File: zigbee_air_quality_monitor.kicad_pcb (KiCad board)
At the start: 2 copper layers, 21 parts, among them J1 USB_C_Receptacle_USB2.0, J2 Conn_02x02_Odd_Even, SW1 PWR_BTN, U1 BT840, U2 PRTR5V0U2F, U3 XC6206P332MR, U4 SCD41-D-R2

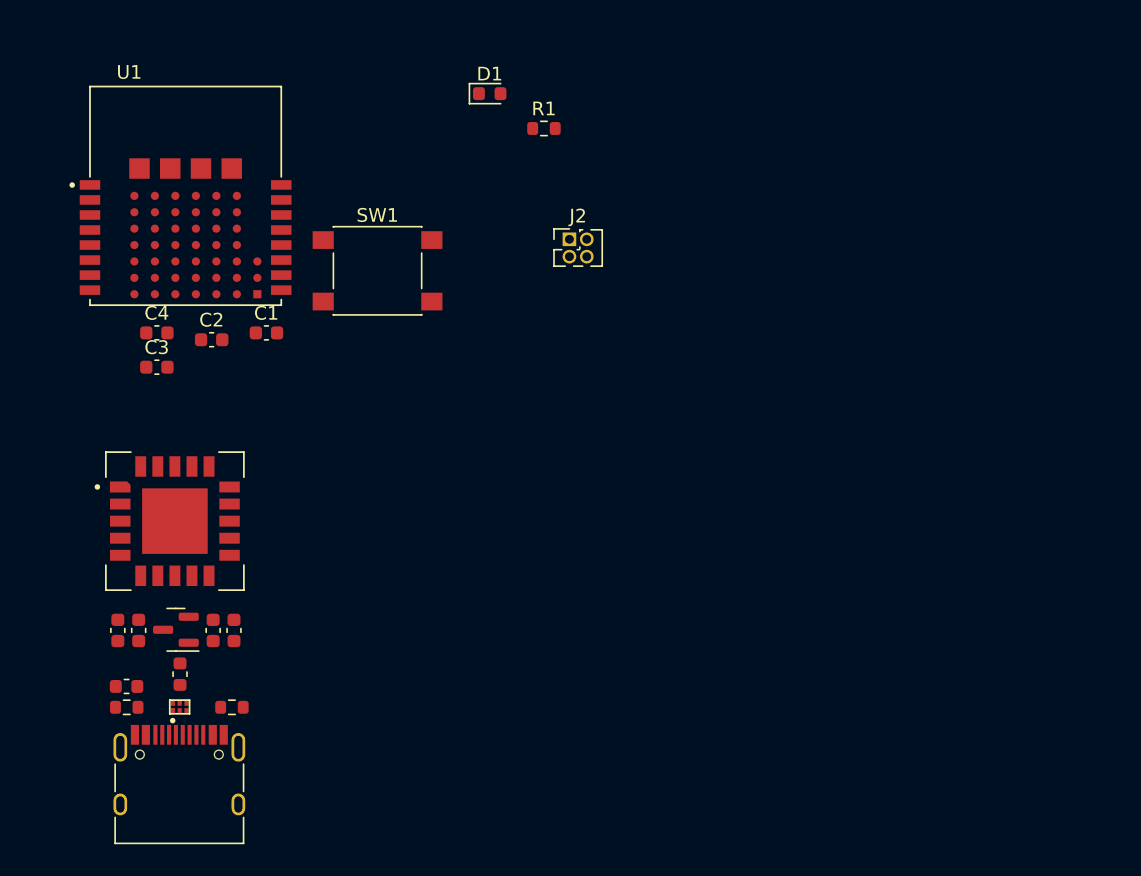
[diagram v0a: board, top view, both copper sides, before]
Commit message: Finished schematics, added 3D models
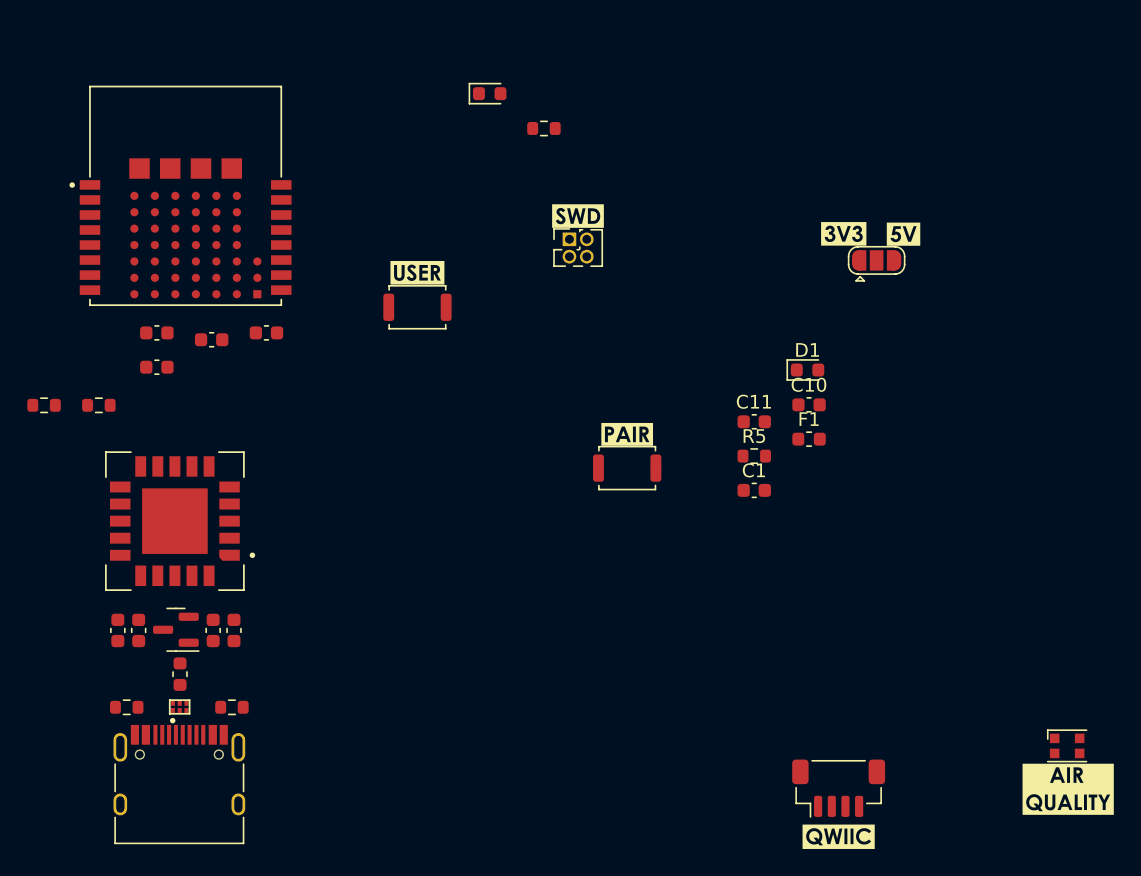
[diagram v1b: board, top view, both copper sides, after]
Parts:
- added C1: 100nF, Capacitor_SMD:C_0603_1608Metric, F.Cu at (174.0, 115.2)
- added C10: 100nF, Capacitor_SMD:C_0603_1608Metric, F.Cu at (178.0, 109.0)
- added C11: 4.7uF, Capacitor_SMD:C_0603_1608Metric, F.Cu at (174.0, 110.2)
- added D1: STATUS_LED, LED_SMD:LED_0603_1608Metric, F.Cu at (177.9, 106.4)
- added D3: WS2812B, LED_SMD:LED_WS2812B-2020_PLCC4_2.0x2.0mm, F.Cu at (196.9, 133.9)
- added J3: QWIIC, Connector_JST:JST_SH_BM04B-SRSS-TB_1x04-1MP_P1.00mm_Vertical, F.Cu at (180.2, 137.0)
- added JP1: SolderJumper_3_Bridged12, Jumper:SolderJumper-3_P1.3mm_Open_RoundedPad1.0x1.5mm, F.Cu at (183.0, 98.4)
- added R3: 5k1, Resistor_SMD:R_0603_1608Metric, F.Cu at (122.0, 109.0)
- added R4: 5k1, Resistor_SMD:R_0603_1608Metric, F.Cu at (126.1, 109.0)
- added R5: 1k, Resistor_SMD:R_0603_1608Metric, F.Cu at (174.0, 112.7)
- added SW2: USER_BTN, Button_Switch_SMD:SW_Push_SPST_NO_Alps_SKRK, F.Cu at (149.4, 101.8)
- added kibuzzard-63D64107: G***, kibuzzard-63D64107, F.Cu at (161.1, 95.2)
- added kibuzzard-63D6450F: G***, kibuzzard-63D6450F, F.Cu at (180.2, 140.6)
- added kibuzzard-63D64589: G***, kibuzzard-63D64589, F.Cu at (197.0, 137.1)
- added kibuzzard-63D645FF: G***, kibuzzard-63D645FF, F.Cu at (180.6, 96.5)
- added kibuzzard-63D6461A: G***, kibuzzard-63D6461A, F.Cu at (184.9, 96.5)
- added kibuzzard-63D64B66: G***, kibuzzard-63D64B66, F.Cu at (149.4, 99.3)
- added kibuzzard-63D64B8B: G***, kibuzzard-63D64B8B, F.Cu at (164.7, 111.1)
- D2: renamed from D1; value STATUS_LED -> PAIRING_LED
- SW1: value PWR_BTN -> PAIR_BTN; footprint Button_Switch_SMD:SW_Push_1P1T_NO_6x6mm_H9.5mm -> Button_Switch_SMD:SW_Push_SPST_NO_Alps_SKRK
- moved F1 53.1 mm to (178.0, 111.5)
- moved SW1 23.3 mm to (164.7, 113.6)
- turned U4 to 180 degrees
- renumbered C1 to C2, C2 to C3, C3 to C4, C4 to C6, C6 to C7, C7 to C8, C8 to C9, R2 to R1, R3 to R2, R1 to R6, U2 to U1, U1 to U2
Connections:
- net Net-(R1-Pad1) renamed /PAIRING_LED
- C2 pad 1: Net-(C1-Pad1) -> Net-(C2-Pad1)
- C5 pad 1: Net-(C5-Pad1) -> VCC
- C7 pad 1: Net-(C5-Pad1) -> VCC
- FB1 pad 2: Net-(C5-Pad1) -> VCC
- SW1 pad 1: Net-(C1-Pad1) -> Net-(U2-Pad5)
- U2 pad 1: unconnected-(U1-Pad1) -> /I2C_SDA
- U2 pad 14: /RESET -> unconnected-(U2-Pad14)
- U2 pad 2: unconnected-(U1-Pad2) -> /I2C_SCL
- U2 pad 4: unconnected-(U1-Pad4) -> /AIR_QUALITY_LED
- U2 pad 5: unconnected-(U1-Pad5) -> Net-(U2-Pad5)
- U2 pad 6: Net-(C1-Pad1) -> Net-(C2-Pad1)
- U2 pad 7: unconnected-(U1-Pad7) -> /STATUS_LED
- U3 pad 3: Net-(C5-Pad1) -> VCC
- U4 pad 10: unconnected-(U4-Pad10) -> /I2C_SDA
- U4 pad 19: unconnected-(U4-Pad19) -> VCC
- U4 pad 20: Net-(U4-Pad20) -> GND
- U4 pad 21: Net-(U4-Pad20) -> GND
- U4 pad 6: Net-(U4-Pad20) -> GND
- U4 pad 7: unconnected-(U4-Pad7) -> VCC
- U4 pad 9: unconnected-(U4-Pad9) -> /I2C_SCL

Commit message: Rough part placement
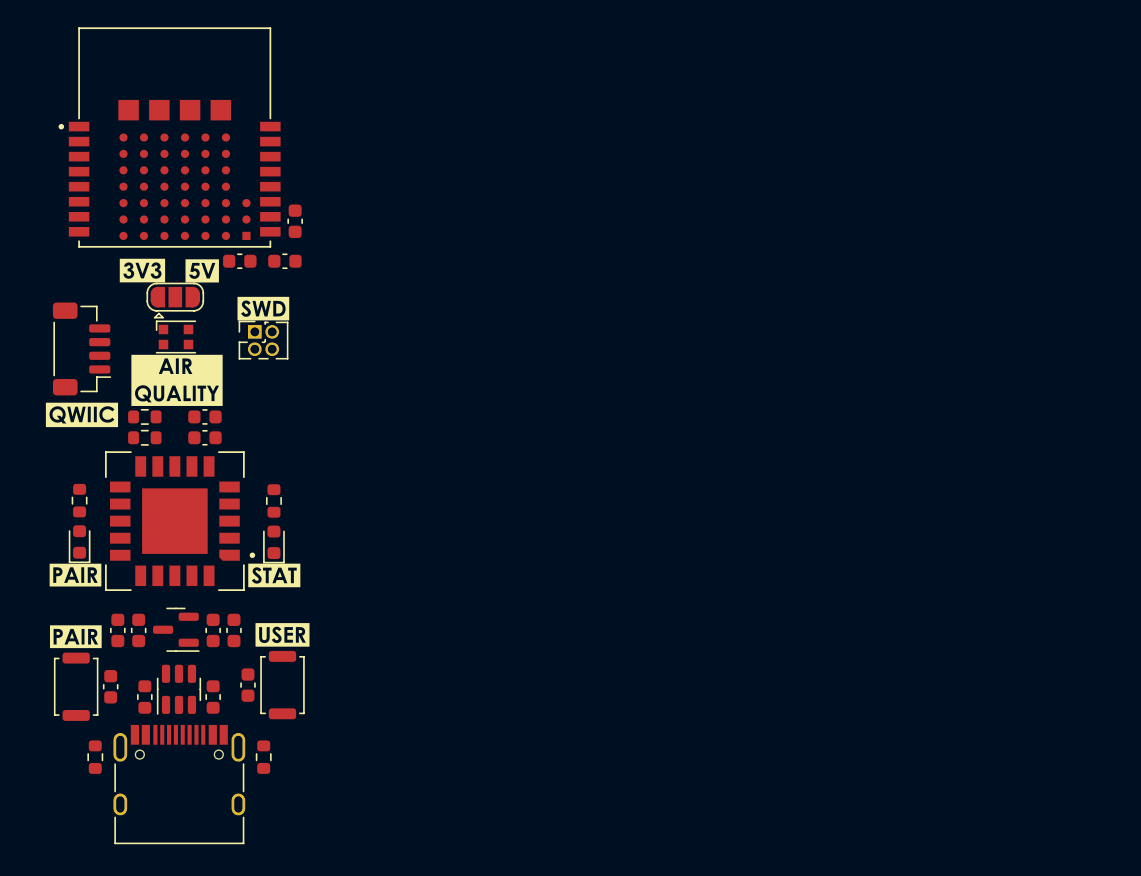
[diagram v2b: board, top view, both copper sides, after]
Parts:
- added kibuzzard-63D64B8B: G***, kibuzzard-63D64B8B, F.Cu at (124.3, 121.4)
- added kibuzzard-63D9ACF8: G***, kibuzzard-63D9ACF8, F.Cu at (138.9, 121.5)
- U1: value PRTR5V0U2F -> USBLC6-2SC6; footprint zigbee_air_quality_monitor:PSON50P145X100X90-6N -> Package_TO_SOT_SMD:SOT-23-6
- moved D3 71.8 mm to (131.7, 104.0)
- moved kibuzzard-63D64589 71.8 mm to (131.8, 107.2)
- moved J2 64.1 mm to (124.8, 104.9), turned to 90 degrees
- moved kibuzzard-63D6450F 63.4 mm to (124.8, 109.7)
- moved F1 52.1 mm to (129.4, 130.3), turned to 90 degrees
- moved JP1 51.4 mm to (131.7, 101.1)
- moved kibuzzard-63D645FF 51.4 mm to (129.2, 99.1)
- moved kibuzzard-63D6461A 51.4 mm to (133.6, 99.2)
- moved C1 49.2 mm to (126.9, 129.6), turned to -90 degrees
- moved D2 44.5 mm to (124.7, 119.0), turned to 90 degrees
- moved C10 44.3 mm to (133.8, 111.4)
- moved R6 43.6 mm to (124.7, 116.0), turned to 90 degrees
- moved SW1 43.4 mm to (124.4, 129.6), turned to -90 degrees
- moved kibuzzard-63D64B8B 43.0 mm to (124.4, 125.9)
- moved D1 41.0 mm to (138.9, 119.0), turned to 90 degrees
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- renumbered J3 to J2, J2 to J3
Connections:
- C3 pad 1: VBUS -> VCC
- U2 pad F6: VBUS -> VCC
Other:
- copper layers 2 -> 4

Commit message: Routing WIP
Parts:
- removed JP1: SolderJumper_3_Bridged12, Jumper:SolderJumper-3_P1.3mm_Open_RoundedPad1.0x1.5mm
- removed kibuzzard-63D645FF: G***, kibuzzard-63D645FF
- removed kibuzzard-63D6461A: G***, kibuzzard-63D6461A
- moved C3 2.80 mm to (136.4, 101.3)
- moved C4 2.80 mm to (140.4, 98.3)
- moved C6 2.80 mm to (139.7, 101.3)
- moved U2 2.80 mm to (131.6, 92.2)
- moved J3 1.12 mm to (137.5, 104.8)
- moved kibuzzard-63D64107 1.12 mm to (138.1, 103.0)
- moved U3 0.50 mm to (131.7, 124.9)
- moved C5 0.50 mm to (127.5, 125.0)
- moved C7 0.50 mm to (129.0, 125.0)
- moved C8 0.50 mm to (134.4, 125.0)
- moved C9 0.50 mm to (135.9, 125.0)
- moved F1 0.50 mm to (129.4, 129.8)
- moved FB1 0.50 mm to (134.4, 129.8)
- moved U1 0.50 mm to (131.9, 129.3)
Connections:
- D3 pad 1: Net-(D3-Pad1) -> +3.3V
- J1 pad A6: /USB_CONN_D- -> /USB_CONN_D+
- J1 pad A7: /USB_CONN_D+ -> /USB_CONN_D-
- J1 pad B6: /USB_CONN_D- -> /USB_CONN_D+
- J1 pad B7: /USB_CONN_D+ -> /USB_CONN_D-
- U1 pad 1: /USB_CONN_D- -> /USB_CONN_D+
- U1 pad 3: /USB_CONN_D+ -> /USB_CONN_D-
- U1 pad 4: /USB_D+ -> /USB_D-
- U1 pad 6: /USB_D- -> /USB_D+
- U2 pad 13: unconnected-(U2-Pad13) -> /STATUS_LED
- U2 pad 14: unconnected-(U2-Pad14) -> /PAIRING_LED
- U2 pad 7: /STATUS_LED -> unconnected-(U2-P0.09/NFC1-Pad7)
- U2 pad 8: /PAIRING_LED -> unconnected-(U2-P0.10/NFC2-Pad8)
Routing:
- net /USB_D-: track 0.00 -> 38.3 mm, vias 0 -> 2
- net /USB_D+: track 0.00 -> 37.2 mm, vias 0 -> 2
- net /USB_CONN_D+: track 0.00 -> 3.03 mm
- net /USB_CONN_D-: track 0.00 -> 3.01 mm
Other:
- board outline added: 19.8 x 50.9 mm

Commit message: CI test
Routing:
- net /USB_CONN_D+: track 3.03 -> 8.30 mm
- net /USB_CONN_D-: track 3.01 -> 7.32 mm, vias 0 -> 2
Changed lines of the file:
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@@
     (stroke (width 0.1) (type default)) (fill none) (layer "Edge.Cuts"))
   (segment (start 132.2 132.027499) (end 132.1475 131.974999) (width 0.23) (layer "F.Cu") (net 9))
+  (segment (start 131.04 134.525) (end 131.2 134.365) (width 0.23) (layer "F.Cu") (net 9))
+  (segment (start 132.2 134.510956) (end 132.2 133.115) (width 0.23) (layer "F.Cu") (net 9))
   (segment (start 132.875 130.7875) (end 132.875 130.425) (width 0.23) (layer "F.Cu") (net 9))
   (segment (start 132.2 133.115) (end 132.2 132.027499) (width 0.23) (layer "F.Cu") (net 9))
   (segment (start 132.54 131.306341) (end 132.54 131.1225) (width 0.23) (layer "F.Cu") (net 9))
   (segment (start 132.1475 131.974999) (end 132.1475 131.698841) (width 0.23) (layer "F.Cu") (net 9))
+  (segment (start 131.2 134.365) (end 131.2 133.115) (width 0.23) (layer "F.Cu") (net 9))
+  (segment (start 132.299279 134.610235) (end 132.2 134.510956) (width 0.23) (layer "F.Cu") (net 9))
   (segment (start 132.1475 131.698841) (end 132.54 131.306341) (width 0.23) (layer "F.Cu") (net 9))
   (segment (start 132.54 131.1225) (end 132.875 130.7875) (width 0.23) (layer "F.Cu") (net 9))
+  (via (at 131.04 134.525) (size 0.7) (drill 0.3) (layers "F.Cu" "B.Cu") (net 9))
+  (via (at 132.299279 134.610235) (size 0.7) (drill 0.3) (layers "F.Cu" "B.Cu") (net 9))
+  (segment (start 131.125235 134.610235) (end 132.299279 134.610235) (width 0.23) (layer "B.Cu") (net 9))
+  (segment (start 131.04 134.525) (end 131.125235 134.610235) (width 0.23) (layer "B.Cu") (net 9))
   (segment (start 131.31 131.1225) (end 130.975 130.7875) (width 0.23) (layer "F.Cu") (net 10))
+  (segment (start 132.004523 135.25) (end 132.6 135.25) (width 0.23) (layer "F.Cu") (net 10))
   (segment (start 131.7275 131.551766) (end 131.31 131.134266) (width 0.23) (layer "F.Cu") (net 10))
+  (segment (start 131.7 133.115) (end 131.67 133.145) (width 0.23) (layer "F.Cu") (net 10))
+  (segment (start 132.95 134.37) (end 132.7 134.12) (width 0.23) (layer "F.Cu") (net 10))
+  (segment (start 132.95 134.9) (end 132.95 134.37) (width 0.23) (layer "F.Cu") (net 10))
+  (segment (start 131.67 134.915477) (end 132.004523 135.25) (width 0.23) (layer "F.Cu") (net 10))
+  (segment (start 132.6 135.25) (end 132.95 134.9) (width 0.23) (layer "F.Cu") (net 10))
+  (segment (start 132.7 134.12) (end 132.7 133.115) (width 0.23) (layer "F.Cu") (net 10))
   (segment (start 130.975 130.7875) (end 130.975 130.425) (width 0.23) (layer "F.Cu") (net 10))
   (segment (start 131.7 133.115) (end 131.7 132.027499) (width 0.23) (layer "F.Cu") (net 10))
   (segment (start 131.7525 131.974999) (end 131.7525 131.85) (width 0.23) (layer "F.Cu") (net 10))
+  (segment (start 131.67 133.145) (end 131.67 134.915477) (width 0.23) (layer "F.Cu") (net 10))
   (segment (start 131.7525 131.85) (end 131.7275 131.825) (width 0.23) (layer "F.Cu") (net 10))
   (segment (start 131.7275 131.825) (end 131.7275 131.551766) (width 0.23) (layer "F.Cu") (net 10))
@@
   (segment (start 131.7 132.027499) (end 131.7525 131.974999) (width 0.23) (layer "F.Cu") (net 10))
   (segment (start 131.578234 127.1725) (end 131.727499 127.1725) (width 0.23) (layer "F.Cu") (net 54))
+  (segment (start 135.79002 97) (end 135.84002 96.95) (width 0.23) (layer "F.Cu") (net 54))
+  (segment (start 136.479216 95.964257) (end 136.244217 95.729258) (width 0.23) (layer "F.Cu") (net 54))
   (segment (start 131.727499 127.15039) (end 131.4925 126.915391) (width 0.23) (layer "F.Cu") (net 54))
+  (segment (start 136.457415 95.964257) (end 136.479216 95.964257) (width 0.23) (layer "F.Cu") (net 54))
+  (segment (start 131.31 127.815) (end 131.31 127.440734) (width 0.23) (layer "F.Cu") (net 54))
+  (segment (start 131.31 127.440734) (end 131.578234 127.1725) (width 0.23) (layer "F.Cu") (net 54))
+  (segment (start 135.84002 96.95) (end 135.84002 96.581652) (width 0.23) (layer "F.Cu") (net 54))
   (segment (start 135.84002 96.581652) (end 136.457415 95.964257) (width 0.23) (layer "F.Cu") (net 54))
-  (segment (start 131.31 127.815) (end 131.31 127.440734) (width 0.23) (layer "F.Cu") (net 54))
-  (segment (start 135.84002 97) (end 135.84002 96.581652) (width 0.23) (layer "F.Cu") (net 54))
-  (segment (start 135.35 97) (end 135.84002 97) (width 0.23) (layer "F.Cu") (net 54))
-  (segment (start 131.31 127.440734) (end 131.578234 127.1725) (width 0.23) (layer "F.Cu") (net 54))
-  (segment (start 136.457415 95.964257) (end 136.479216 95.964257) (width 0.23) (layer "F.Cu") (net 54))
   (segment (start 130.975 128.15) (end 131.31 127.815) (width 0.23) (layer "F.Cu") (net 54))
-  (segment (start 136.479216 95.964257) (end 136.244217 95.729258) (width 0.23) (layer "F.Cu") (net 54))
+  (segment (start 135.35 97) (end 135.79002 97) (width 0.23) (layer "F.Cu") (net 54))
   (segment (start 131.727499 127.1725) (end 131.727499 127.15039) (width 0.23) (layer "F.Cu") (net 54))
   (via (at 131.4925 126.915391) (size 0.7) (drill 0.3) (layers "F.Cu" "B.Cu") (net 54))
@@
   (segment (start 134.1525 124.255391) (end 132.1225 126.285391) (width 0.23) (layer "B.Cu") (net 54))
   (segment (start 136.479217 95.964258) (end 136.479217 100.291475) (width 0.23) (layer "B.Cu") (net 54))
+  (segment (start 135.35 98.2) (end 136.235 97.315) (width 0.23) (layer "F.Cu") (net 55))
+  (segment (start 136.874218 95.964257) (end 137.109217 95.729258) (width 0.23) (layer "F.Cu") (net 55))
   (segment (start 136.595258 96.385) (end 136.874218 96.385) (width 0.23) (layer "F.Cu") (net 55))
-  (segment (start 136.235 97.254742) (end 136.235 96.745258) (width 0.23) (layer "F.Cu") (net 55))
   (segment (start 132.54 127.815) (end 132.54 127.440734) (width 0.23) (layer "F.Cu") (net 55))
   (segment (start 136.874218 96.385) (end 136.874218 95.964257) (width 0.23) (layer "F.Cu") (net 55))
@@
   (segment (start 132.875 128.15) (end 132.54 127.815) (width 0.23) (layer "F.Cu") (net 55))
   (segment (start 132.54 127.440734) (end 132.271766 127.1725) (width 0.23) (layer "F.Cu") (net 55))
-  (segment (start 135.35 98.2) (end 136.265129 97.284871) (width 0.23) (layer "F.Cu") (net 55))
-  (segment (start 136.265129 97.284871) (end 136.235 97.254742) (width 0.23) (layer "F.Cu") (net 55))
-  (segment (start 136.874218 95.964257) (end 137.109217 95.729258) (width 0.23) (layer "F.Cu") (net 55))
   (segment (start 136.235 96.745258) (end 136.595258 96.385) (width 0.23) (layer "F.Cu") (net 55))
   (segment (start 132.271766 127.1725) (end 132.122501 127.1725) (width 0.23) (layer "F.Cu") (net 55))
   (segment (start 132.122501 127.15039) (end 132.3575 126.915391) (width 0.23) (layer "F.Cu") (net 55))
+  (segment (start 136.235 97.315) (end 136.235 96.745258) (width 0.23) (layer "F.Cu") (net 55))
   (via (at 132.3575 126.915391) (size 0.7) (drill 0.3) (layers "F.Cu" "B.Cu") (net 55))
   (via (at 137.109217 95.729258) (size 0.7) (drill 0.3) (layers "F.Cu" "B.Cu") (net 55))
